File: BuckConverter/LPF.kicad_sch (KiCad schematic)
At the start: 7 parts, among them U1 LM358

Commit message: PCB Completed
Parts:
- renumbered R4 to R3, R3 to R4
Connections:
- net +3.3V: now also U1.8 (V+)
- net GND: now also R1.1
- net IN: now also R4.2
- net at C1.1, R3.1, R4.1: now also U1.3 (+); no longer U1.2 (-)
- net at R1.2: now also R2.1, U1.2 (-)
- net VFLIT: now reaches U1.1
- net VFLIT: now also R2.2; no longer R2.1
- no-connect marks 0 -> 3
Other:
- moved on the sheet: R1, R2
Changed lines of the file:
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@@
 		(color 0 0 0 0)
+	)
+	(no_connect
+		(at 120.65 96.52)
+	)
+	(no_connect
+		(at 135.89 93.98)
+	)
+	(no_connect
+		(at 120.65 91.44)
 	)
 	(wire
@@
 	(wire
 		(pts
+			(xy 77.47 45.72) (xy 81.28 45.72)
+		)
+		(stroke
+			(width 0)
+			(type default)
+		)
+	)
+	(wire
+		(pts
 			(xy 100.33 29.21) (xy 100.33 40.64)
 		)
@@
 		(pts
 			(xy 106.68 29.21) (xy 100.33 29.21)
+		)
+		(stroke
+			(width 0)
+			(type default)
+		)
+	)
+	(wire
+		(pts
+			(xy 29.21 31.75) (xy 30.48 31.75)
+		)
+		(stroke
+			(width 0)
+			(type default)
+		)
+	)
+	(wire
+		(pts
+			(xy 81.28 40.64) (xy 82.55 40.64)
+		)
+		(stroke
+			(width 0)
+			(type default)
+		)
+	)
+	(wire
+		(pts
+			(xy 33.02 78.74) (xy 33.02 80.01)
 		)
 		(stroke
@@
 				(size 1.27 1.27)
 			)
+		)
+	)
+	(label "VFLIT"
+		(at 120.65 43.18 0)
+		(effects
+			(font
+				(size 1.27 1.27)
+			)
+			(justify left bottom)
+		)
+	)
+	(label "IN"
+		(at 27.94 36.83 0)
+		(effects
+			(font
+				(size 1.27 1.27)
+			)
+			(justify left bottom)
+		)
+	)
+	(label "OUT"
+		(at 49.53 31.75 180)
+		(effects
+			(font
+				(size 1.27 1.27)
+			)
+			(justify right bottom)
+		)
+	)
+	(label "IN"
+		(at 77.47 45.72 180)
+		(effects
+			(font
+				(size 1.27 1.27)
+			)
+			(justify right bottom)
 		)
 	)
@@
 	(hierarchical_label "IN"
 		(shape input)
-		(at 29.21 36.83 180)
+		(at 27.94 36.83 180)
 		(effects
 			(font
@@
 	)
 	(symbol
+		(lib_id "power:GND")
+		(at 81.28 40.64 270)
+		(unit 1)
+		(exclude_from_sim no)
+		(in_bom yes)
+		(on_board yes)
+		(dnp no)
+		(property "Reference" "#PWR054"
+			(at 74.93 40.64 0)
+			(effects
+				(font
+					(size 1.27 1.27)
+				)
+				(hide yes)
+			)
+		)
+		(property "Value" "GND"
+			(at 77.724 40.64 90)
+			(effects
+				(font
+					(size 1.27 1.27)
+				)
+				(justify right)
+			)
+		)
+		(property "Footprint" ""
+			(at 81.28 40.64 0)
+			(effects
+				(font
+					(size 1.27 1.27)
+				)
+				(hide yes)
+			)
+		)
+		(property "Datasheet" ""
+			(at 81.28 40.64 0)
+			(effects
+				(font
+					(size 1.27 1.27)
+				)
+				(hide yes)
+			)
+		)
+		(property "Description" "Power symbol creates a global label with name \"GND\" , ground"
+			(at 81.28 40.64 0)
+			(effects
+				(font
+					(size 1.27 1.27)
+				)
+				(hide yes)
+			)
+		)
+		(pin "1"
+		)
+		(instances
+			(project "BuckConverter"
+				(path "/fd6bac42-b74a-4329-b064-b676c79abc2c/3b7721cc-2c2d-455e-a8f7-184f5b45c1dc"
+					(reference "#PWR054")
+					(unit 1)
+				)
+			)
+		)
+	)
+	(symbol
 		(lib_id "Device:R")
 		(at 93.98 53.34 0)
@@
 		(dnp no)
 		(fields_autoplaced yes)
-		(property "Reference" "R4"
+		(property "Reference" "R3"
 			(at 96.52 52.0699 0)
 			(effects
@@
 			(project "BuckConverter"
 				(path "/fd6bac42-b74a-4329-b064-b676c79abc2c/3b7721cc-2c2d-455e-a8f7-184f5b45c1dc"
-					(reference "R4")
+					(reference "R3")
 					(unit 1)
 				)
@@
 	(symbol
 		(lib_id "Device:R")
-		(at 86.36 40.64 270)
+		(at 86.36 40.64 90)
 		(unit 1)
 		(exclude_from_sim no)
@@
 		)
 		(property "Footprint" "Resistor_SMD:R_0805_2012Metric"
-			(at 86.36 38.862 90)
+			(at 86.36 42.418 90)
 			(effects
 				(font
@@
 	(symbol
 		(lib_id "Device:R")
-		(at 110.49 29.21 270)
+		(at 110.49 29.21 90)
 		(unit 1)
 		(exclude_from_sim no)
@@
 		)
 		(property "Footprint" "Resistor_SMD:R_0805_2012Metric"
-			(at 110.49 27.432 90)
+			(at 110.49 30.988 90)
 			(effects
 				(font
@@
 	)
 	(symbol
+		(lib_name "LM358_2")
 		(lib_id "Amplifier_Operational:LM358")
 		(at 111.76 43.18 0)
@@
 		(on_board yes)
 		(dnp no)
-		(property "Reference" "R3"
+		(property "Reference" "R4"
 			(at 83.058 43.688 90)
 			(effects
@@
 			(project "BuckConverter"
 				(path "/fd6bac42-b74a-4329-b064-b676c79abc2c/3b7721cc-2c2d-455e-a8f7-184f5b45c1dc"
-					(reference "R3")
+					(reference "R4")
 					(unit 1)
 				)
@@
 		(fields_autoplaced yes)
 		(property "Reference" "U1"
-			(at 128.27 83.82 0)
+			(at 128.016 87.122 0)
 			(effects
 				(font
@@
 		)
 		(property "Value" "LM358"
-			(at 128.27 86.36 0)
+			(at 128.27 89.154 0)
 			(effects
 				(font
@@
 	)
 	(symbol
+		(lib_name "LM358_1")
 		(lib_id "Amplifier_Operational:LM358")
 		(at 35.56 87.63 0)
@@
 		(fields_autoplaced yes)
 		(property "Reference" "U1"
-			(at 34.29 86.3599 0)
-			(effects
-				(font
-					(size 1.27 1.27)
-				)
-				(justify left)
+			(at 35.306 80.772 0)
+			(effects
+				(font
+					(size 1.27 1.27)
+				)
 			)
 		)
 		(property "Value" "LM358"
-			(at 34.29 88.8999 0)
-			(effects
-				(font
-					(size 1.27 1.27)
-				)
-				(justify left)
-			)
-		)
+			(at 35.56 82.804 0)
+			(effects
+				(font
+					(size 1.27 1.27)
+				)
+			)
+		)

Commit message: LPF updates
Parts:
- R1: value 10000 -> 10k
- R2, R3: value ? -> 500; footprint Resistor_SMD:R_0805_2012Metric -> Resistor_SMD:R_0603_1608Metric; Part Number RMCF0805FT10K0 -> RT0603BRC07500RL
- R4: value ? -> 10k
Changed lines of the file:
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@@
 			)
 		)
-		(property "Value" "?"
+		(property "Value" "500"
 			(at 96.52 54.6099 0)
 			(effects
@@
 			)
 		)
-		(property "Footprint" "Resistor_SMD:R_0805_2012Metric"
+		(property "Footprint" "Resistor_SMD:R_0603_1608Metric"
 			(at 92.202 53.34 90)
 			(effects
@@
 			)
 		)
-		(property "Part Number" "RMCF0805FT10K0"
+		(property "Part Number" "RT0603BRC07500RL"
 			(at 93.98 53.34 0)
 			(effects
@@
 			)
 		)
-		(property "Value" "10000"
+		(property "Value" "10k"
 			(at 86.36 36.83 90)
 			(effects
@@
 			)
 		)
-		(property "Value" "?"
+		(property "Value" "500"
 			(at 110.49 25.4 90)
 			(effects
@@
 			)
 		)
-		(property "Footprint" "Resistor_SMD:R_0805_2012Metric"
+		(property "Footprint" "Resistor_SMD:R_0603_1608Metric"
 			(at 110.49 30.988 90)
 			(effects
@@
 			)
 		)
-		(property "Part Number" "RMCF0805FT10K0"
+		(property "Part Number" "RT0603BRC07500RL"
 			(at 110.49 29.21 0)
 			(effects
@@
 		(dnp no)
 		(property "Reference" "R4"
-			(at 83.058 43.688 90)
-			(effects
-				(font
-					(size 1.27 1.27)
-				)
-			)
-		)
-		(property "Value" "?"
-			(at 85.598 43.688 90)
-			(effects
-				(font
+			(at 85.09 48.006 90)
+			(effects
+				(font
+					(size 1.27 1.27)
+				)
+			)
+		)
+		(property "Value" "10k"
+			(at 85.09 50.038 90)
+			(effects
+				(font

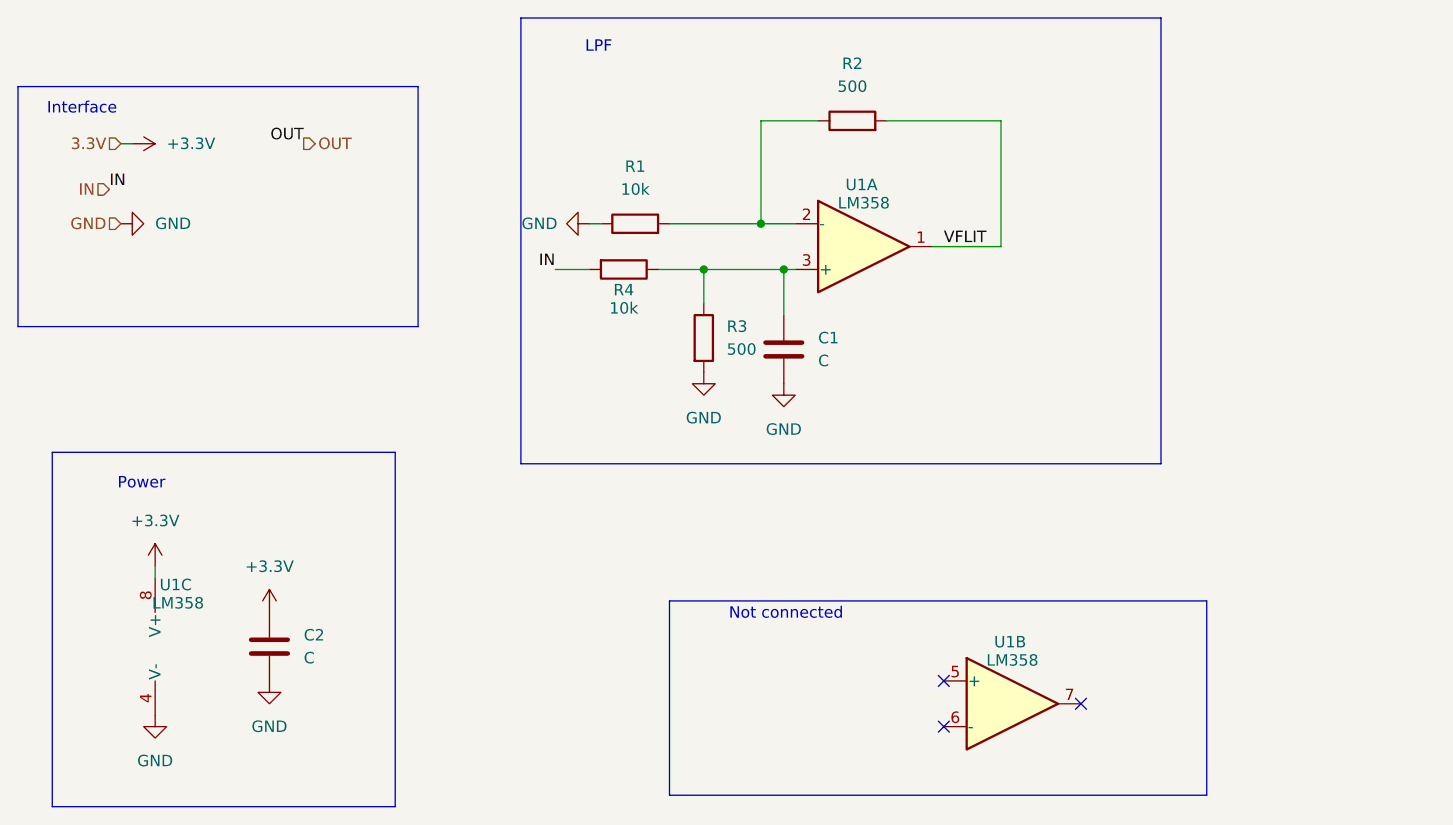
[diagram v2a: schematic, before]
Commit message: PCB updated LC footprints
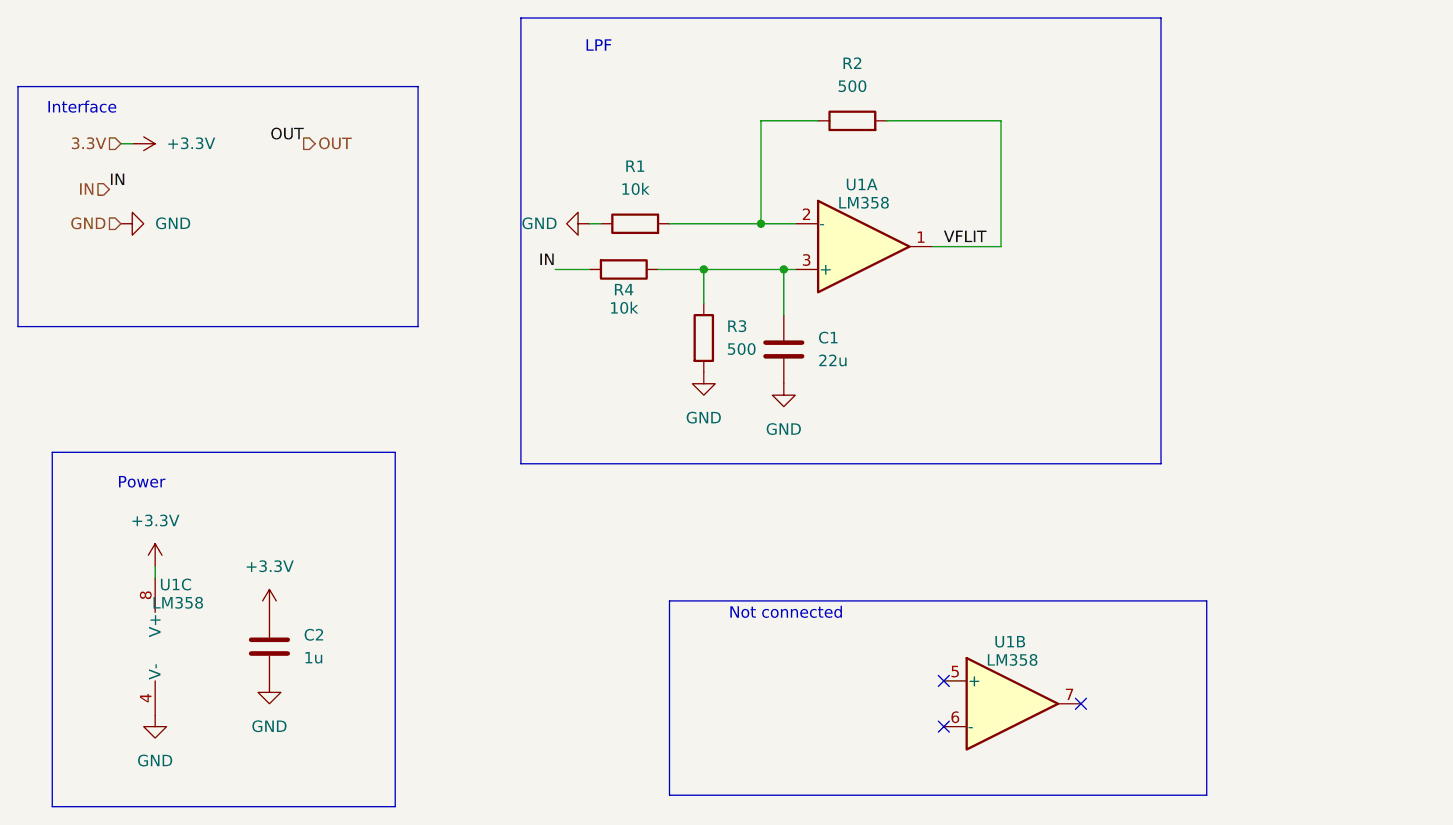
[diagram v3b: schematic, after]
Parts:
- C1: value C -> 22u; Part Number (none) -> C2012X5R1V226M125AC
- C2: value C -> 1u
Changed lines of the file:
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@@
 			)
 		)
-		(property "Value" "C"
+		(property "Value" "22u"
 			(at 106.68 55.8799 0)
 			(effects
@@
 			)
 		)
-		(property "Part Number" ""
+		(property "Part Number" "C2012X5R1V226M125AC"
 			(at 102.87 54.61 0)
 			(effects
@@
 			)
 		)
-		(property "Value" "C"
+		(property "Value" "1u"
 			(at 49.53 88.8999 0)
 			(effects

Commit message: Update PCB and BOM
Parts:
- removed U1: LM358, Package_SO:VSSOP-8_3x3mm_P0.65mm, symbol Amplifier_Operational:LM358
- added U1: LM358AP, P8, symbol LM358AP:LM358AP
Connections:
- net +3.3V: now also U1.8 (VCC)
- net GND: now also U1.4 (GND)
- net VFLIT: now also U1.1 (1OUT)
- net at C1.1, R3.1, R4.1: now also U1.3 (1IN+)
- net at R1.2, R2.1: now also U1.2 (1IN-)
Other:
- note removed: "Not connected"
- moved on the sheet: C1, C2, R1, R2, R3, R4
